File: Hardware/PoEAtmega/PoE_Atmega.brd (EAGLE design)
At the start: 85.2 x 72.4 mm, 59 parts, among them IC2 ATMEGA32U4-MU, U2 SPX3819-3.3, U4 W5500, X1 J1011F21P, X3 microUSB, Y2 CRYSTAL-GROUNDEDSMD-3.2X2.5, Y4 8MHz

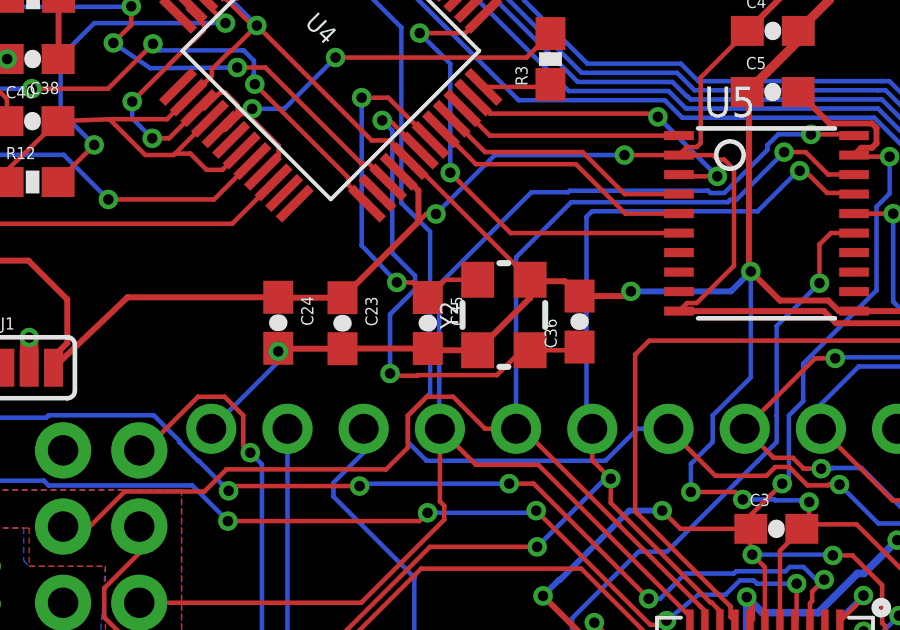
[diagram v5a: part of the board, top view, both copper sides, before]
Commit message: HEEP-508 added 25mhz value to wiznet xtal
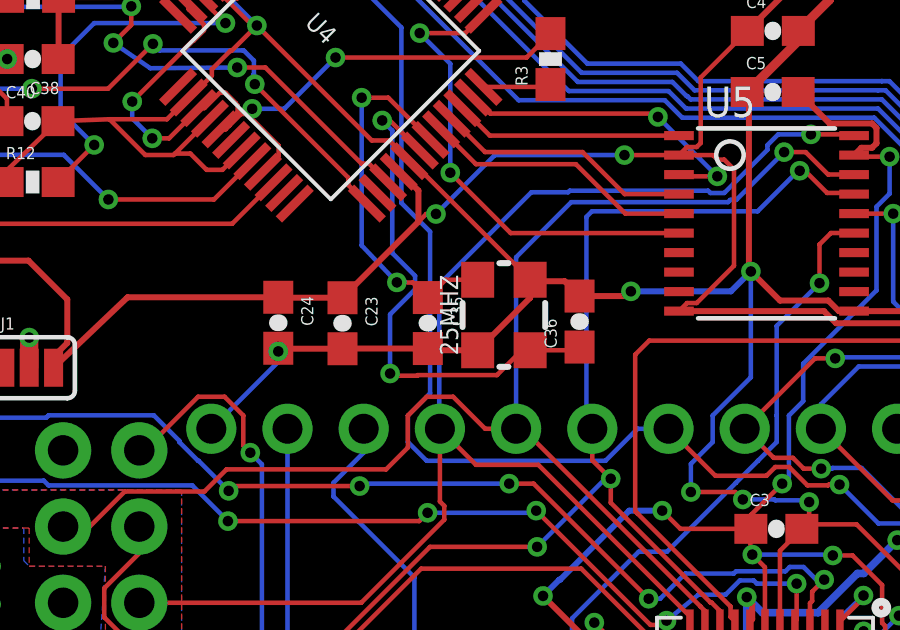
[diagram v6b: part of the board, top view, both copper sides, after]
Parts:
- renumbered Y2 to 25MHZ
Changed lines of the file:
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@@
 <attribute name="VALUE" x="24.513459375" y="51.59725625" size="0.4064" layer="27" font="vector"/>
 </element>
-<element name="Y2" library="SparkFun-Clocks" package="CRYSTAL-SMD-3.2X2.5MM" value="CRYSTAL-GROUNDEDSMD-3.2X2.5" x="41.223525" y="40.122140625" smashed="yes" rot="R90">
+<element name="25MHZ" library="SparkFun-Clocks" package="CRYSTAL-SMD-3.2X2.5MM" value="CRYSTAL-GROUNDEDSMD-3.2X2.5" x="41.223525" y="40.122140625" smashed="yes" rot="R90">
 <attribute name="NAME" x="39.699525" y="40.122140625" size="0.6096" layer="25" font="vector" ratio="20" rot="R90" align="bottom-center"/>
 <attribute name="VALUE" x="42.747525" y="40.122140625" size="0.6096" layer="27" font="vector" ratio="20" rot="R90" align="top-center"/>
@@
 <contactref element="C10" pad="2"/>
 <contactref element="C11" pad="2"/>
-<contactref element="Y2" pad="2"/>
-<contactref element="Y2" pad="4"/>
+<contactref element="25MHZ" pad="2"/>
+<contactref element="25MHZ" pad="4"/>
 <contactref element="X3" pad="SPRT@2"/>
 <contactref element="X3" pad="BASE@1"/>
@@
 <contactref element="U4" pad="31"/>
 <contactref element="C35" pad="1"/>
-<contactref element="Y2" pad="3"/>
+<contactref element="25MHZ" pad="3"/>
 <wire x1="39.280675" y1="41.297140625" x2="38.687509375" y2="40.703975" width="0.1524" layer="1"/>
 <wire x1="39.280675" y1="41.297140625" x2="40.348525" y2="41.297140625" width="0.1524" layer="1"/>
@@
 <signal name="N$26">
 <contactref element="C36" pad="1"/>
-<contactref element="Y2" pad="1"/>
+<contactref element="25MHZ" pad="1"/>
 <contactref element="U4" pad="30"/>
 <wire x1="43.639953125" y1="38.947140625" x2="42.098525" y2="38.947140625" width="0.1524" layer="1"/>
